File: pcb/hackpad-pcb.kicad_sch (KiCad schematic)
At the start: 33 parts, among them U1 MCU_Seeed_XIAO_RP2040

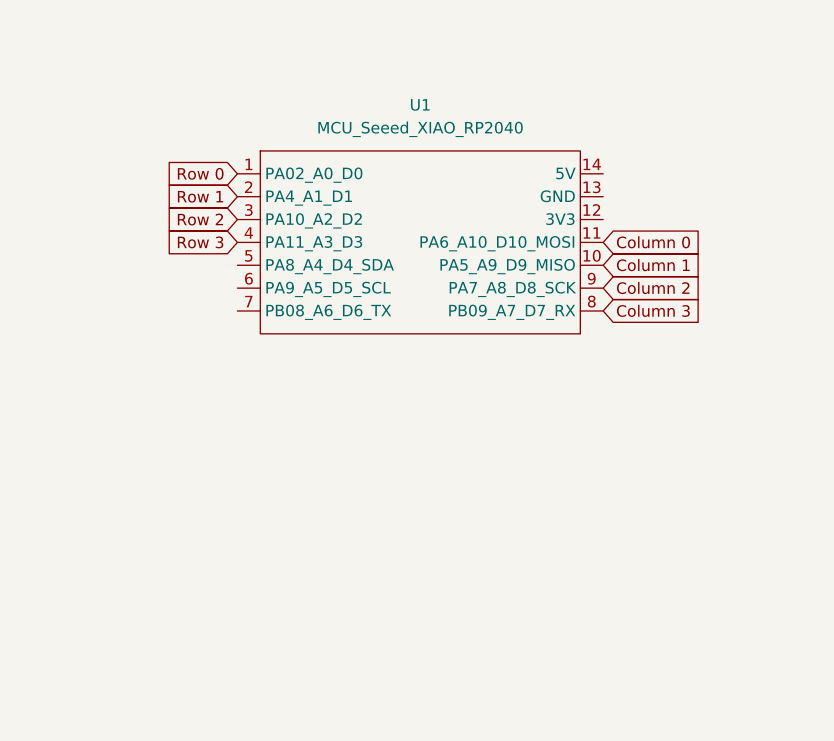
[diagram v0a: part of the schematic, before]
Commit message: Moved diodes and added OLED
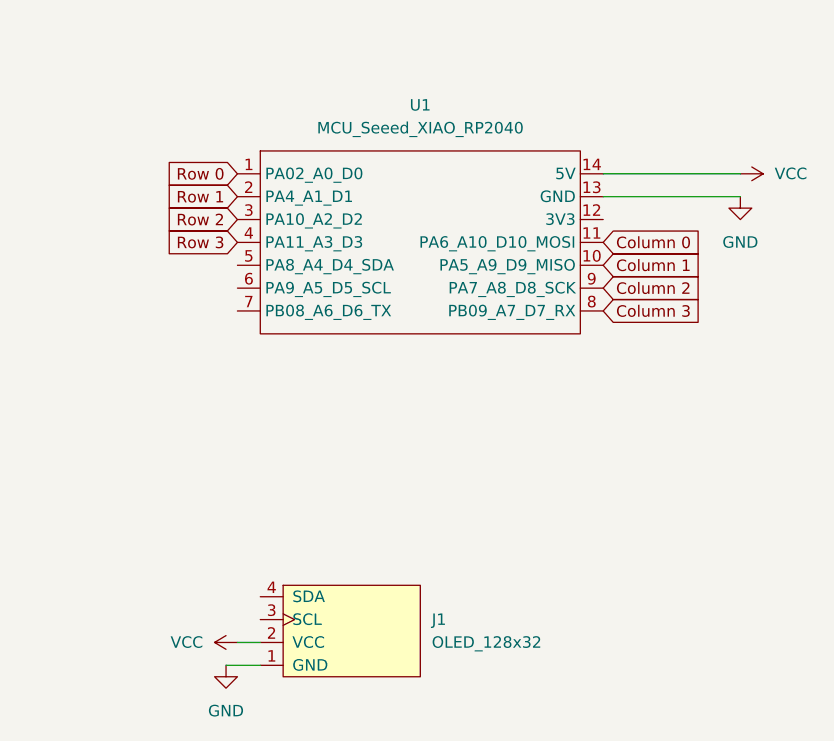
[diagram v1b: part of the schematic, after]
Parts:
- added J1: OLED_128x32, ScottoKeebs_Components:OLED_128x32, symbol ScottoKeebs:OLED_128x32
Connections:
- net GND: now reaches U1.13 (GND)
- net GND: now also J1.1 (GND)
- net VCC: now reaches U1.14 (5V)
- net VCC: now also J1.2 (VCC)

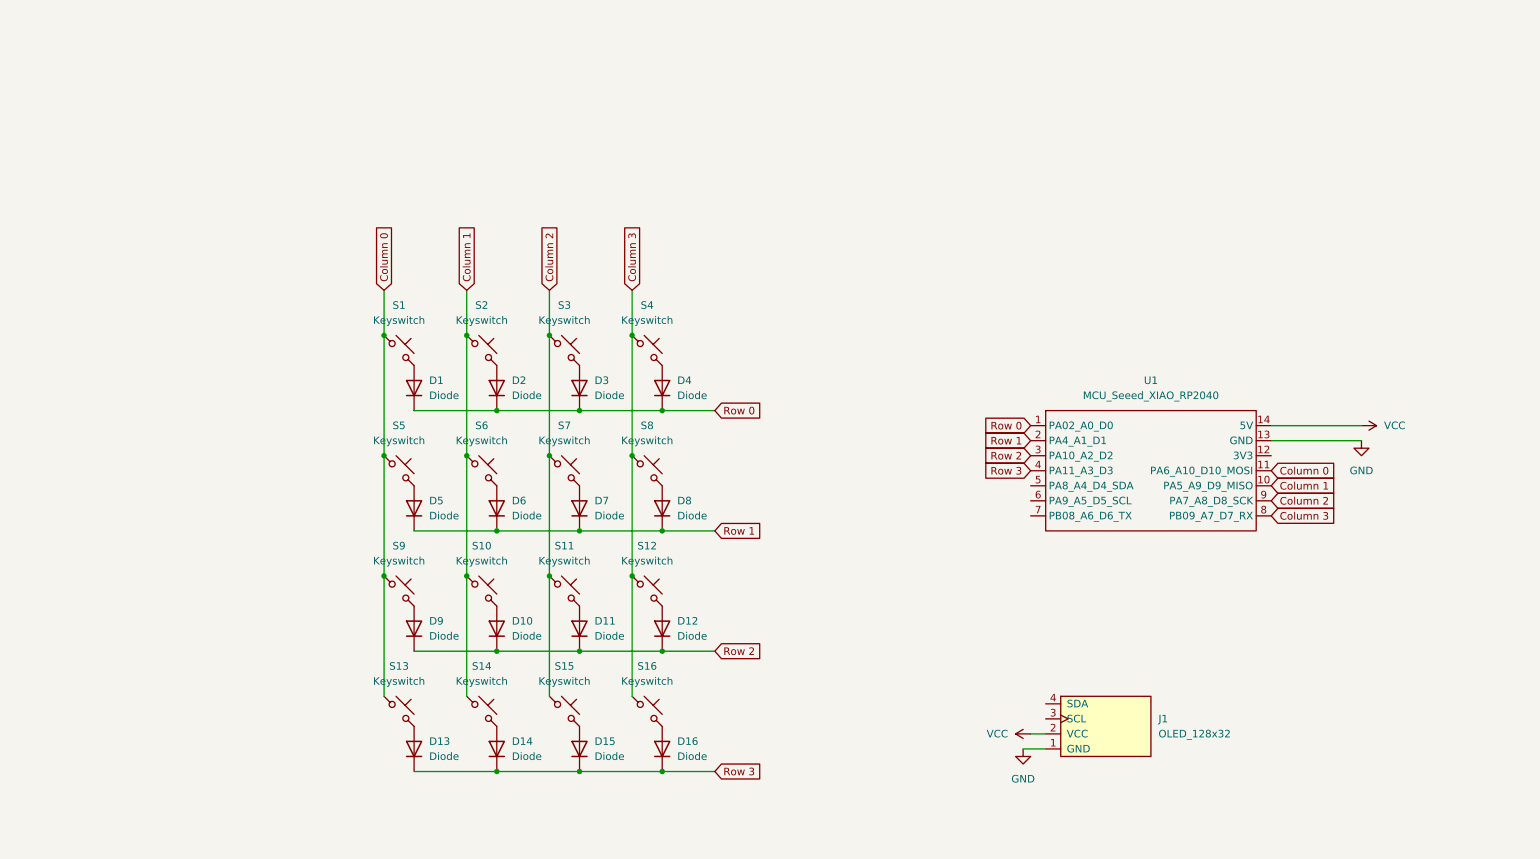
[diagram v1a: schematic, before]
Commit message: Routed a little bit more
Signed-off-by: Urjith Mishra <66270347+TheScientist101@users.noreply.github.com>
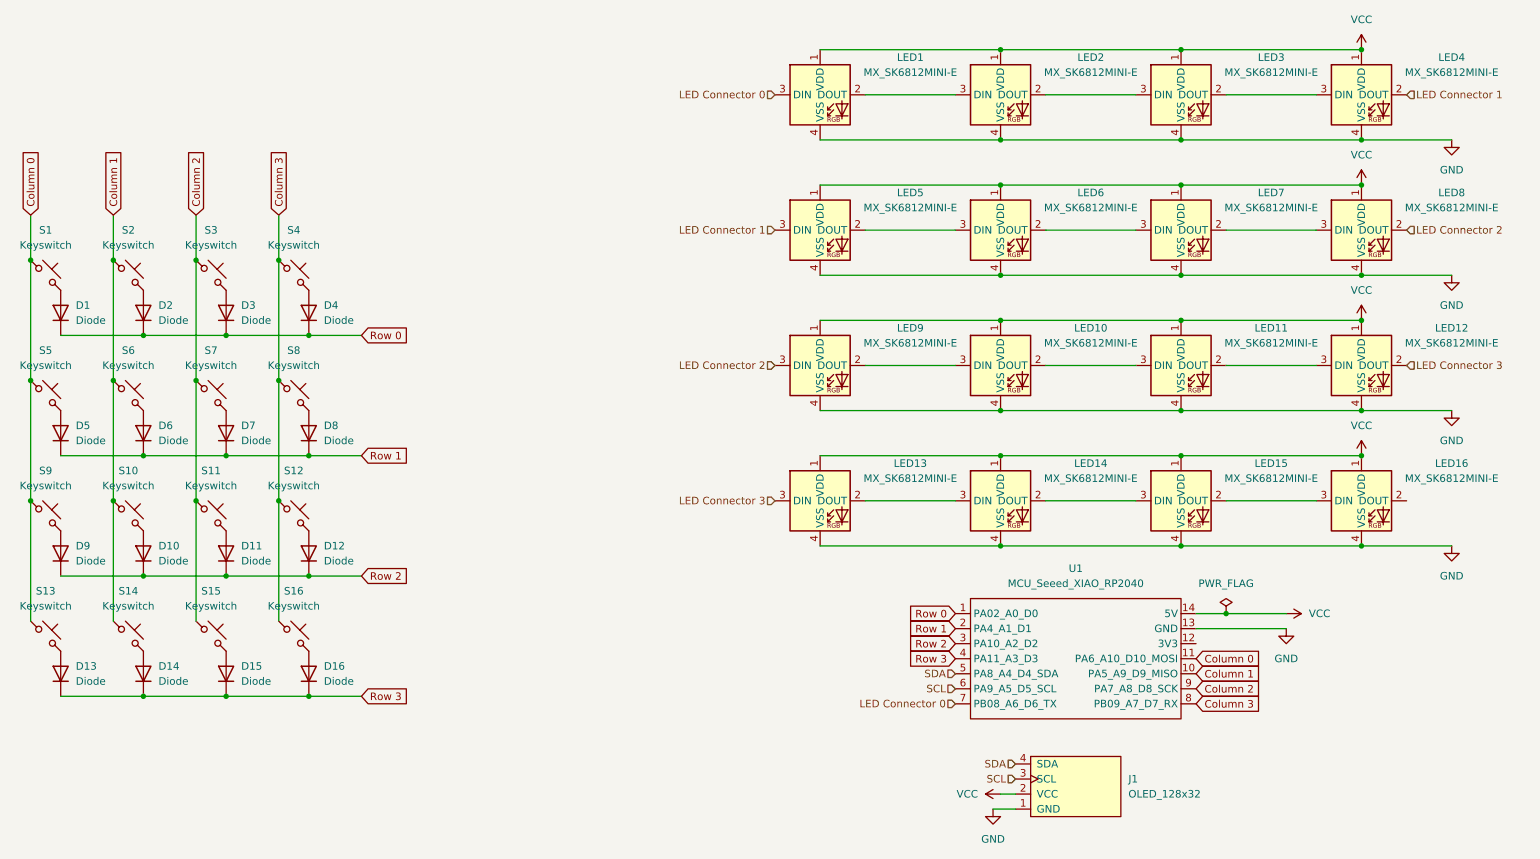
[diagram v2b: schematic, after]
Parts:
- added LED1, LED10, LED11, LED12, LED13, LED14, LED15, LED16, LED2, LED3, LED4, LED5, LED6, LED7, LED8, LED9: MX_SK6812MINI-E, PCM_marbastlib-mx:LED_MX_6028R, symbol PCM_marbastlib-mx:MX_SK6812MINI-E
- S1, S10, S11, S12, S13, S14, S15, S16, S2, S3, S4, S5, S6, S7, S8, S9: footprint ScottoKeebs_MX:MX_PCB_1.00u -> ScottoKeebs_MX:MX_Plate_1.00u
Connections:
- net GND: now also LED1.4 (VSS), LED10.4 (VSS), LED11.4 (VSS), LED12.4 (VSS), LED13.4 (VSS), LED14.4 (VSS), LED15.4 (VSS), LED16.4 (VSS), LED2.4 (VSS), LED3.4 (VSS), LED4.4 (VSS), LED5.4 (VSS), LED6.4 (VSS), LED7.4 (VSS), LED8.4 (VSS), LED9.4 (VSS)
- net VCC: now also LED1.1 (VDD), LED10.1 (VDD), LED11.1 (VDD), LED12.1 (VDD), LED13.1 (VDD), LED14.1 (VDD), LED15.1 (VDD), LED16.1 (VDD), LED2.1 (VDD), LED3.1 (VDD), LED4.1 (VDD), LED5.1 (VDD), LED6.1 (VDD), LED7.1 (VDD), LED8.1 (VDD), LED9.1 (VDD)
- net SDA: now reaches U1.5 (PA8_A4_D4_SDA)
- net SDA: now also J1.4 (SDA)
- net SCL: now reaches U1.6 (PA9_A5_D5_SCL)
- net SCL: now also J1.3 (SCL)
- net LED Connector 0: now reaches U1.7 (PB08_A6_D6_TX)
- net LED Connector 0: now also LED1.3 (DIN)
- new net: LED10.2 (DOUT), LED11.3 (DIN)
- new net: LED10.3 (DIN), LED9.2 (DOUT)
- new net: LED11.2 (DOUT), LED12.3 (DIN)
- new net: LED13.2 (DOUT), LED14.3 (DIN)
- new net: LED1.2 (DOUT), LED2.3 (DIN)
- new net: LED3.2 (DOUT), LED4.3 (DIN)
- new net: LED14.2 (DOUT), LED15.3 (DIN)
- new net: LED15.2 (DOUT), LED16.3 (DIN)
- new net: LED2.2 (DOUT), LED3.3 (DIN)
- new net: LED6.2 (DOUT), LED7.3 (DIN)
- new net: LED5.2 (DOUT), LED6.3 (DIN)
- new net: LED7.2 (DOUT), LED8.3 (DIN)
- new net LED Connector 1: LED4.2 (DOUT), LED5.3 (DIN)
- new net LED Connector 2: LED8.2 (DOUT), LED9.3 (DIN)
- new net LED Connector 3: LED12.2 (DOUT), LED13.3 (DIN)
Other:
- moved on the sheet: D1, D10, D11, D12, D13, D14, D15, D16, D2, D3, D4, D5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
